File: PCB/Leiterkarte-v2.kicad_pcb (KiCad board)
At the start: 4 copper layers, 100 x 70 mm, 117 parts, among them U501 LMV321

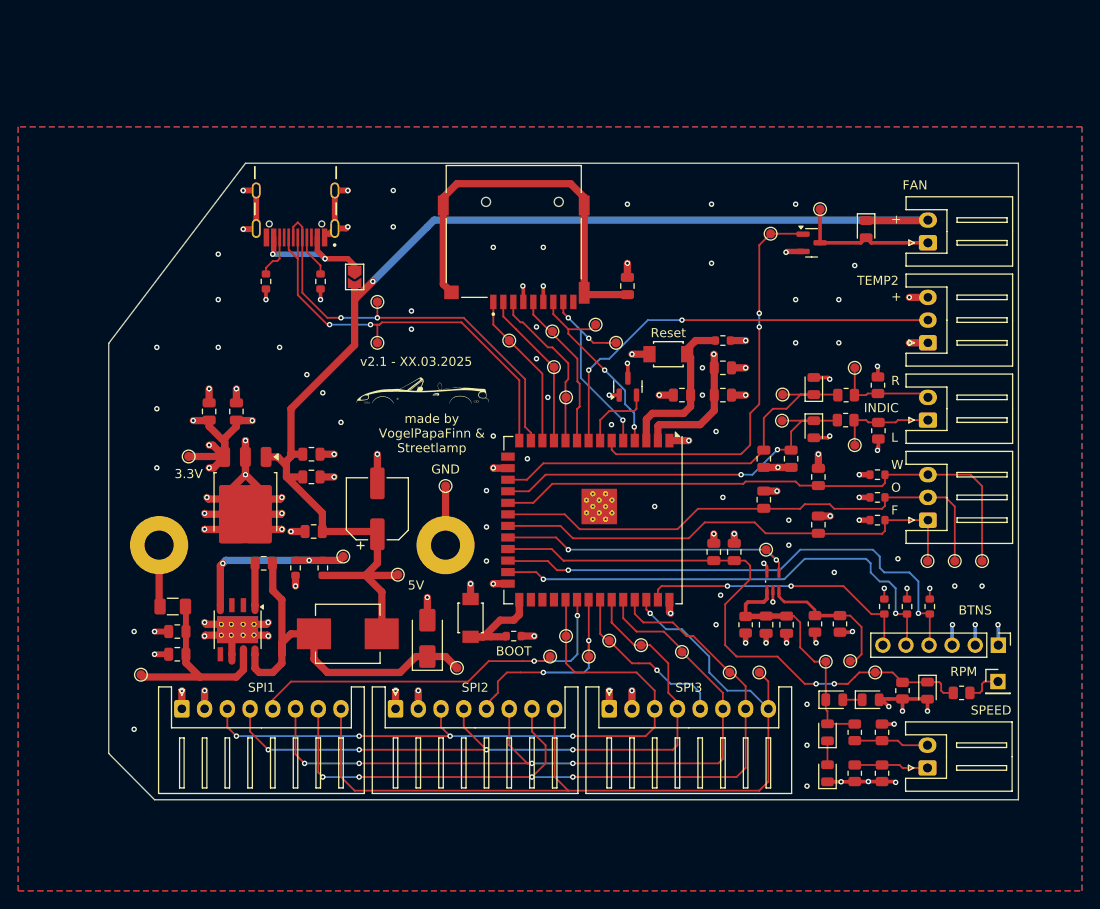
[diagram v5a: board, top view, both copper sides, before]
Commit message: Changed some resistor and capacitor values;Added additional input electrolytic cap;Selected LCSC parts;Added diode footprint;Removed 3.3V power supply and decreased the output of the 5V supply to 3.3V;Added flyback diode on the fan circuit;Added LDO between the USB-C VBUS and the 5V rail
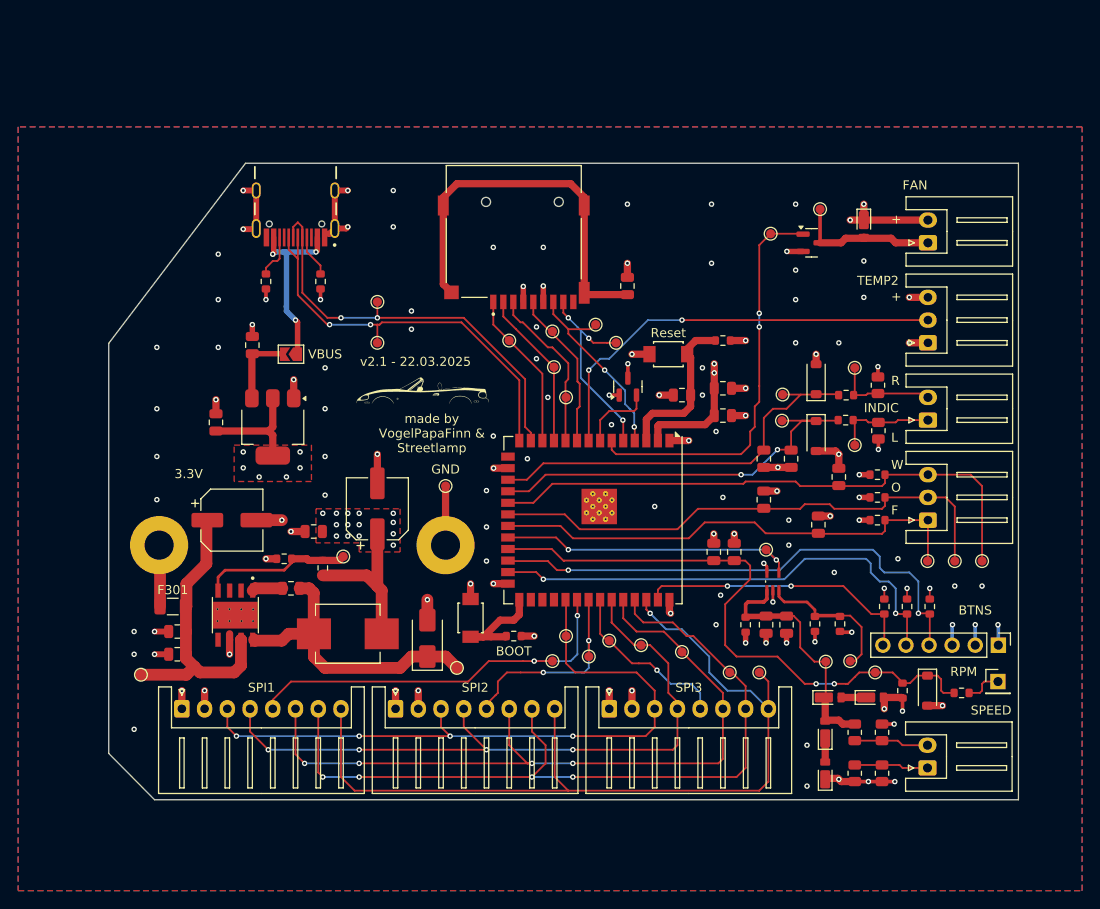
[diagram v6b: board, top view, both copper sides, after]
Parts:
- removed Cin304: 22uF, Capacitor_SMD:C_0805_2012Metric
- removed Cout303: 220uF, Capacitor_SMD:CP_Elec_6.3x5.9
- removed Cout304: C, Capacitor_SMD:C_0805_2012Metric
- removed TP304, TP619: TestPoint_Small, TestPoint:TestPoint_Pad_D1.0mm
- removed V301: LD39150DT33, Package_TO_SOT_SMD:TO-252-3_TabPin2
- added C601: 10uF, Capacitor_SMD:C_0805_2012Metric, F.Cu at (95.8, 65.0)
- added C602: 22uF, Capacitor_SMD:C_0805_2012Metric, F.Cu at (91.8, 73.5)
- added U601: AMS1117-3.3, Package_TO_SOT_SMD:SOT-223-3_TabPin2, F.Cu at (98.0, 74.0)
- 5V301: value TPS5430DDA -> TPS5430DDAR; footprint Package_SO:TI_SO-PowerPAD-8_ThermalVias -> TPS5430DDAR:CONV_TPS5430DDAR
- Cesp202: value 0.1uF -> 10nF
- Cin301: value C -> 220uF; footprint Capacitor_SMD:C_0805_2012Metric -> Capacitor_SMD:CP_Elec_6.3x7.7
- Cin302: value 1uF -> C
- Cin303: value C -> 22uF
- Cout301: value 2.2uF -> 220uF; footprint Capacitor_SMD:C_0805_2012Metric -> Capacitor_SMD:CP_Elec_6.3x5.9
- D301: value .55V 5A -> B340A
- D401, D402, D403: footprint Diode_SMD:D_0805_2012Metric -> Diode_SMD:D_SOD-123
- D501, D502, D503, D504, D601: footprint Diode_SMD:D_0805_2012Metric -> customFootprints:SOD-323HE
- F301: value 2A -> 1.1 polyfuse 2.2A
- R401, R404, R405, R406, R506, R507: footprint Resistor_SMD:R_0805_2012Metric -> Resistor_SMD:R_0603_1608Metric
- R402, R403, R503, R504: value 40k -> 47k
- R501, R502: value 100k -> 200k
- R505: value R -> 10k; footprint Resistor_SMD:R_0805_2012Metric -> Resistor_SMD:R_0603_1608Metric
- Rfbb301: value 3.24k -> 5.9k
- moved TP618 61.4 mm to (158.2, 50.0)
- moved TP615 50.9 mm to (109.5, 64.8)
- moved TP617 50.6 mm to (152.8, 52.8)
- moved TP610 48.5 mm to (148.2, 101.0)
- moved TP616 45.1 mm to (109.5, 60.2)
- moved TP601 33.5 mm to (130.2, 97.0)
- moved TP602 28.5 mm to (138.5, 98.0)
- moved Cin302 24.5 mm to (87.5, 96.5)
- moved TP614 22.8 mm to (128.8, 99.8)
- moved TP608 20.7 mm to (128.9, 67.4)
- moved TP302 20.2 mm to (105.8, 88.2)
- moved Cout301 18.8 mm to (109.5, 83.0)
- moved Cout302 17.5 mm to (102.5, 85.5), turned to 0 degrees
- moved TP303 17.5 mm to (118.2, 100.5)
- moved TP613 15.6 mm to (132.8, 99.2)
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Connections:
- 5V301 pad 4: Net-(5V301-VSENSE) -> VSENSE
- Cin301 pad 1: +5V -> VCC
- Cin302 pad 1: +5V -> GND
- Cin302 pad 2: GND -> VCC
- Cin303 pad 1: GND -> VCC
- Cin303 pad 2: VCC -> GND
- Cout302 pad 1: +3.3V -> GND
- Cout302 pad 2: GND -> +3.3V
- D601 pad 1: +5V -> +3.3V
- Fan601 pad 2: +5V -> +3.3V
- JP601 pad 2: +5V -> Net-(JP601-B)
- L301 pad 2: +5V -> +3.3V
- Rfbb301 pad 1: Net-(5V301-VSENSE) -> VSENSE
- Rfbt301 pad 1: Net-(5V301-VSENSE) -> VSENSE
- Rfbt301 pad 2: +5V -> +3.3V
- TP302 pad 1: +3.3V -> VSENSE
- TP303 pad 1: Net-(5V301-VSENSE) -> Net-(5V301-PH)
- TP601 pad 1: /MCU/SD_CLK -> /MCU/DIN
- TP602 pad 1: /MCU/SD_CMD -> /MCU/CLK
- TP603 pad 1: /MCU/SD_DAT0 -> /MCU/SD_CLK
- TP604 pad 1: /MCU/SD_DAT1 -> /MCU/SD_CMD
- TP605 pad 1: /MCU/SD_DAT2 -> /MCU/SD_DAT0
- TP606 pad 1: /MCU/SD_DAT3 -> /MCU/SD_DAT1
- TP607 pad 1: /MCU/USB_D+ -> /MCU/SD_DAT2
- TP608 pad 1: /MCU/USB_D- -> /MCU/SD_DAT3
- TP609 pad 1: /MCU/DIN -> /MCU/DC
- TP610 pad 1: /MCU/FanControl -> /MCU/RST
- TP611 pad 1: /MCU/CLK -> /MCU/BL
- TP612 pad 1: /MCU/DC -> /MCU/CS3
- TP613 pad 1: /MCU/RST -> /MCU/CS2
- TP614 pad 1: /MCU/BL -> /MCU/CS1
- TP615 pad 1: Net-(D601-A) -> /MCU/USB_D+
- TP616 pad 1: /MCU/CS3 -> /MCU/USB_D-
- TP617 pad 1: /MCU/CS2 -> /MCU/FanControl
- TP618 pad 1: +5V -> Net-(D601-A)
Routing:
- net +5V: track 137.8 -> 0.00 mm, vias 1 -> 0
- net GND: track 154.9 -> 115.4 mm, vias 122 -> 112
- net Net-(5V301-VSENSE): track 20.4 -> 0.00 mm, vias 2 -> 0
- net +3.3V: track 62.8 -> 82.5 mm, vias 21 -> 40
- net VSENSE: track 0.00 -> 16.6 mm
- net VCC: track 22.4 -> 32.5 mm
- net Net-(5V301-PH): track 43.1 -> 34.3 mm
- net Net-(JP601-B): track 0.00 -> 8.34 mm
- net Net-(JP601-A): track 14.6 -> 20.2 mm, vias 2 -> 3
- net Net-(5V301-BOOT): track 5.19 -> 3.36 mm
- net /MCU/RIndicator: track 45.8 -> 44.6 mm
- net /MCU/RPM: track 66.5 -> 67.3 mm
- net Net-(D503-A): track 2.12 -> 2.85 mm
- added copper zone on F.Cu, net +3.3V
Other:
- board text added: "VBUS"
- board text added: "v2.1 - 22.03.2025"
- board text removed: "5V"
- board text removed: "v2.1 - XX.03.2025"
